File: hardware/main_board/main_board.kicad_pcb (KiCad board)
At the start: 4 copper layers, 50 x 50 mm, 80 parts, among them J1 USB Port, J2 I2C, J3 LED, J4 Left_Mic, J5 Left_Speaker, J6 Right_Mic, J7 Right_Speaker, J8 I2C, Q1 MMBT3904, Q2 MMBT3904, SW1 SW_Push, SW2 SW_Push, SW3 SW_Push, U1 AMS1117-3.3, U2 CH340K, U4 Headphone Jack, U5 WM8988LGECN/V, U6 WM8988LGECN/V, U7 AMS1117-3.3, U8 ESP32-WROOM-32E

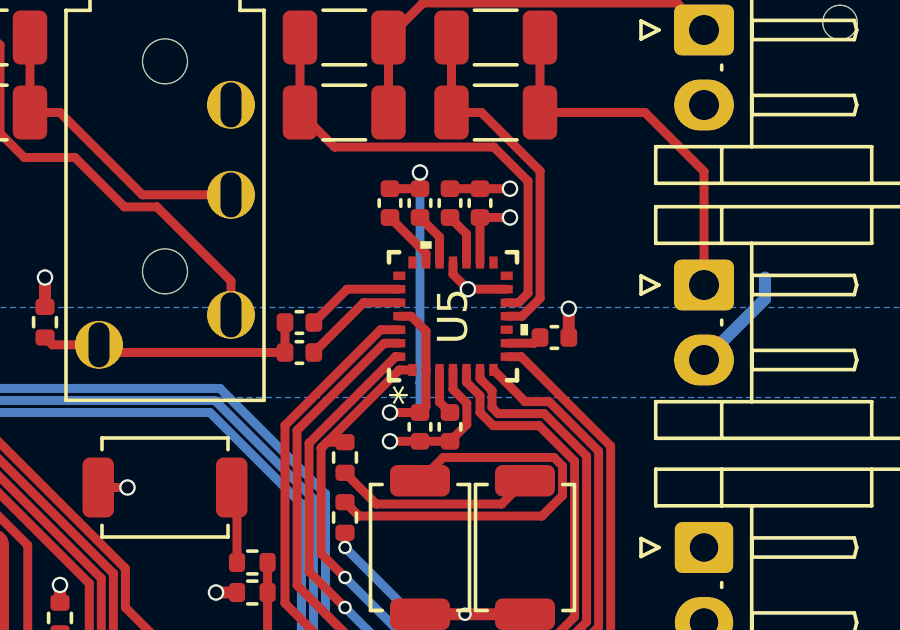
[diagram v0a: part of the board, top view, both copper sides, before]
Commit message: fix: unconnected traces
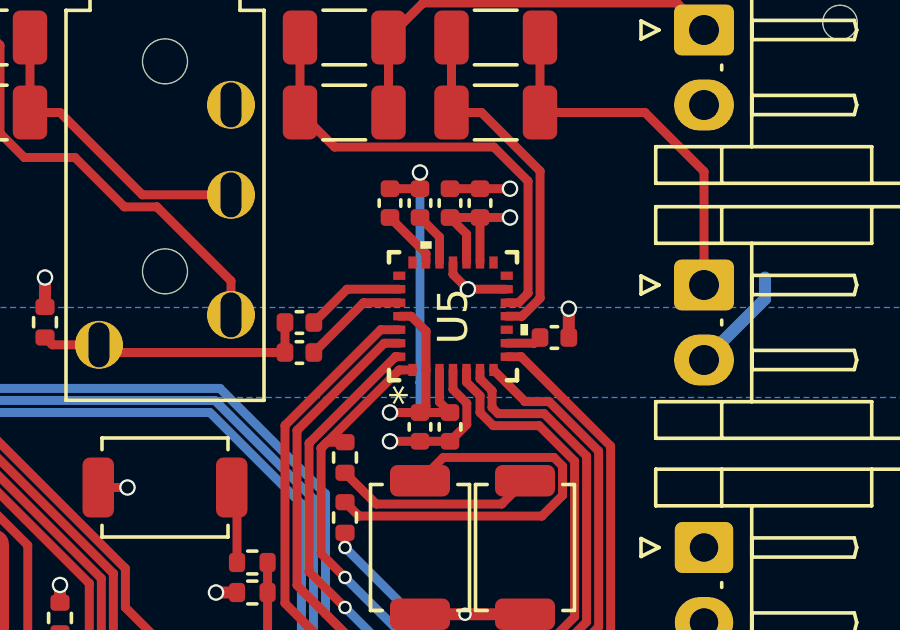
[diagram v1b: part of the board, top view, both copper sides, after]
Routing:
- net +3V3D: track 71.2 -> 72.2 mm
- net +3V3A: track 43.1 -> 44.1 mm
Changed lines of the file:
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@@
+	)
+	(segment
+		(start 156.5 91.5)
+		(end 157.5 91.5)
+		(width 0.3)
+		(layer "F.Cu")
+		(net 1)
 	)
 	(segment
@@
 		(layer "F.Cu")
 		(net 5)
+	)
+	(segment
+		(start 157.5 85)
+		(end 158.5 85)
+		(width 0.3)
+		(layer "F.Cu")
+		(net 5)
